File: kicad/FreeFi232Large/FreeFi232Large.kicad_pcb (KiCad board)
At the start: 2 copper layers, 40.6 x 53.3 mm, 165 parts, among them J1 DB25-Female, J2 3V3-SERIAL, J3 HWFLOW, J4 USB_OTG, J5 ALT-POWER, SW1 B3S-1100, U1 MAX3237, U2 ESP-12E, U3 LM1117-3.3

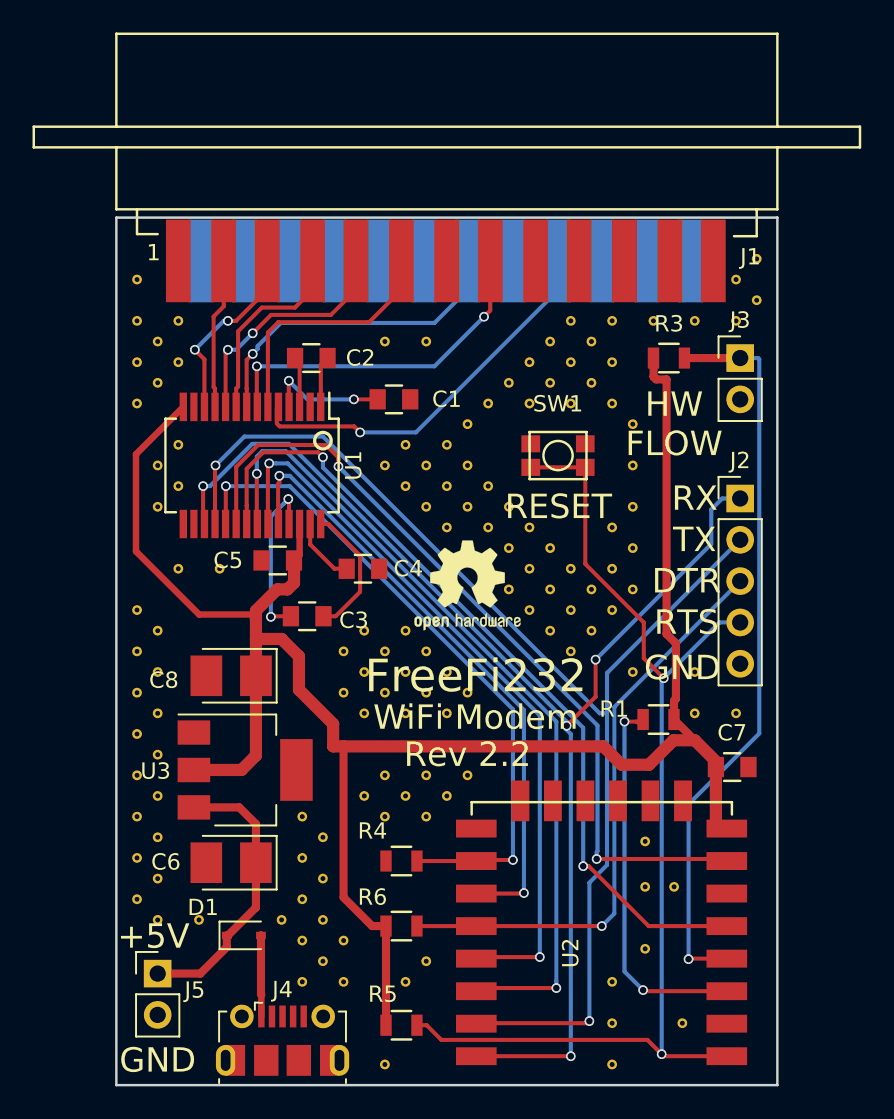
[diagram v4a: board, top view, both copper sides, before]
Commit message: Schematic corrections - pullup added on RX programming port, GPIOs adjusted.
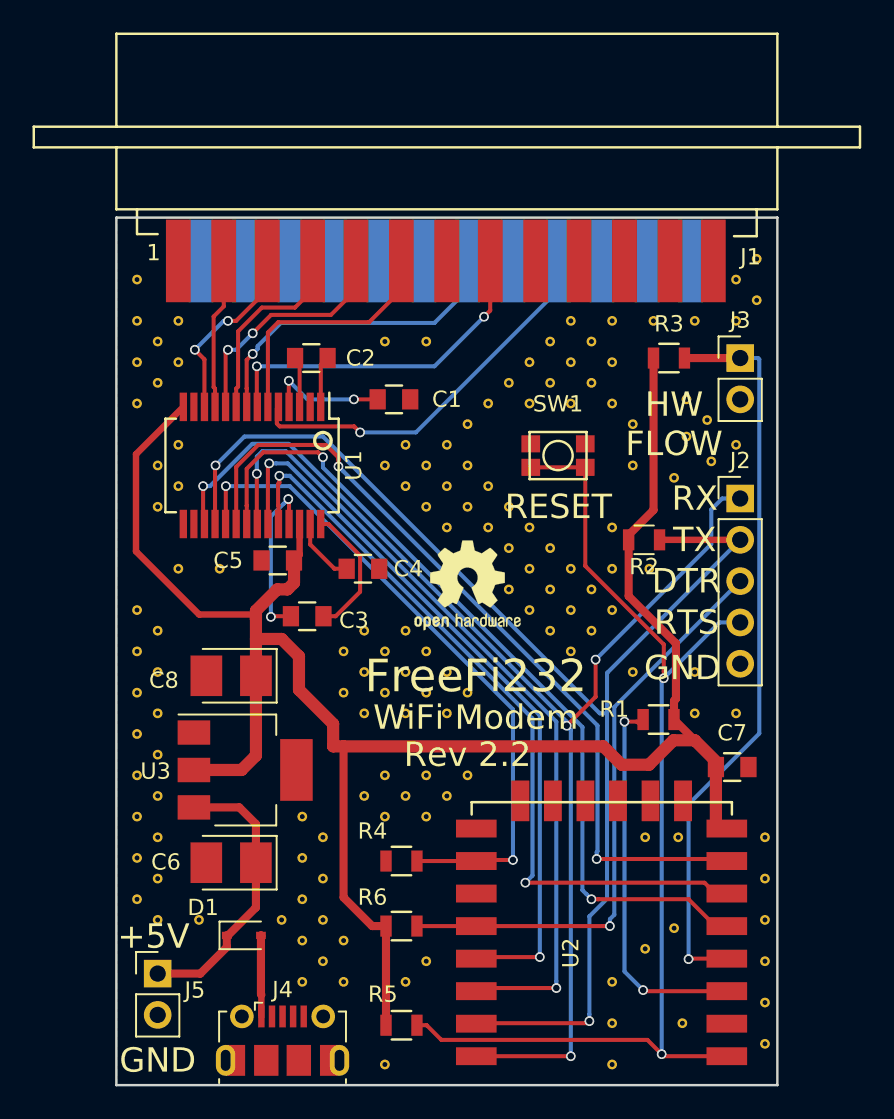
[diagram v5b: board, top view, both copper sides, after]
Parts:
- removed the REF** at (161.3, 101.6)
- removed the REF** at (161.3, 99.1)
- removed the REF** at (161.3, 96.5)
- removed the REF** at (162.1, 117.1)
- removed the REF** at (163.8, 119.9)
- removed the REF** at (162.1, 119.9)
- added R2: 10K, Resistors_SMD:R_0805, F.Cu at (162.0, 98.6)
- added REF**: VIA-0.6mm, stitchingVIA:VIA-0.6mm, F.Cu at (163.8, 122.4)
- added REF**: VIA-0.6mm, stitchingVIA:VIA-0.6mm, F.Cu at (163.8, 94.7)
- added REF**: VIA-0.6mm, stitchingVIA:VIA-0.6mm, F.Cu at (166.1, 93.7)
- added REF**: VIA-0.6mm, stitchingVIA:VIA-0.6mm, F.Cu at (167.6, 92.7)
- added REF**: VIA-0.6mm, stitchingVIA:VIA-0.6mm, F.Cu at (165.9, 91.2)
- added REF**: VIA-0.6mm, stitchingVIA:VIA-0.6mm, F.Cu at (164.6, 92.2)
- added REF**: VIA-0.6mm, stitchingVIA:VIA-0.6mm, F.Cu at (164.6, 89.9)
- added REF**: VIA-0.6mm, stitchingVIA:VIA-0.6mm, F.Cu at (162.3, 100.3)
- added REF**: VIA-0.6mm, stitchingVIA:VIA-0.6mm, F.Cu at (164.1, 116.8)
- added REF**: VIA-0.6mm, stitchingVIA:VIA-0.6mm, F.Cu at (162.1, 116.8)
- added REF**: VIA-0.6mm, stitchingVIA:VIA-0.6mm, F.Cu at (169.4, 116.8)
- added REF**: VIA-0.6mm, stitchingVIA:VIA-0.6mm, F.Cu at (169.4, 129.5)
- added REF**: VIA-0.6mm, stitchingVIA:VIA-0.6mm, F.Cu at (169.4, 127.0)
- added REF**: VIA-0.6mm, stitchingVIA:VIA-0.6mm, F.Cu at (169.4, 124.5)
- added REF**: VIA-0.6mm, stitchingVIA:VIA-0.6mm, F.Cu at (169.4, 121.9)
- added REF**: VIA-0.6mm, stitchingVIA:VIA-0.6mm, F.Cu at (169.4, 119.4)
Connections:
- U1 pad 24: GPIO2 -> GPIO12
- U2 pad 11: GPIO2 -> Net-(U2-Pad11)
- U2 pad 6: Net-(U2-Pad6) -> GPIO12
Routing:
- net GPIO12: track 0.00 -> 47.0 mm, vias 0 -> 2
- net GPIO2: track 37.5 -> 0.00 mm, vias 2 -> 0
- net RXD0: track 75.2 -> 80.2 mm
- net +3V3: track 122.9 -> 123.8 mm
- net GPIO14: track 50.1 -> 51.0 mm

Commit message: Error corrected in schematic and PCB. Gerbers updated.
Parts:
- added REF**: VIA-0.6mm, stitchingVIA:VIA-0.6mm, F.Cu at (152.4, 92.7)
- added REF**: VIA-0.6mm, stitchingVIA:VIA-0.6mm, F.Cu at (156.2, 96.5)
- added REF**: VIA-0.6mm, stitchingVIA:VIA-0.6mm, F.Cu at (162.6, 96.3)
- moved REF** 5.24 mm to (165.1, 96.5)
- moved REF** 4.82 mm to (164.6, 98.8)
- moved REF** 0.92 mm to (160.5, 93.5)
- moved R2 0.13 mm to (162.1, 98.6)
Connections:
- R2 pad 2: +3V3 -> GND
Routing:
- net RXD0: track 80.2 -> 75.2 mm
- net +3V3: track 123.8 -> 125.2 mm
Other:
- board text added: "Rev 2.4"
- board text removed: "Rev 2.2"
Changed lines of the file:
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@@
 (kicad_pcb (version 4) (host pcbnew 4.0.7)
   (general
-    (links 217)
-    (no_connects 0)
+    (links 227)
+    (no_connects 1)
     (area 124.184999 67.161999 175.535001 139.277001)
     (thickness 1.6)
     (drawings 19)
-    (tracks 329)
+    (tracks 330)
     (zones 0)
-    (modules 176)
+    (modules 179)
     (nets 58)
   )
@@
   )
   (setup
-    (last_trace_width 0.25)
+    (last_trace_width 0.5)
     (user_trace_width 0.4)
     (user_trace_width 0.5)
@@
   )
   (module stitchingVIA:VIA-0.6mm (layer F.Cu)
+    (at 152.4 92.71)
+    (zone_connect 2)
+    (fp_text reference REF** (at 0 0.5) (layer F.SilkS) hide
+      (effects (font (size 1 1) (thickness 0.15)))
+    )
+    (fp_text value VIA-0.6mm (at 0 -0.5) (layer F.Fab) hide
+      (effects (font (size 1 1) (thickness 0.15)))
+    )
+    (pad 1 thru_hole circle (at 0 0) (size 0.6 0.6) (drill 0.3) (layers *.Cu)
+      (net 5 GND) (zone_connect 2))
+  )
+  (module stitchingVIA:VIA-0.6mm (layer F.Cu)
+    (at 156.21 96.52)
+    (zone_connect 2)
+    (fp_text reference REF** (at 0 0.5) (layer F.SilkS) hide
+      (effects (font (size 1 1) (thickness 0.15)))
+    )
+    (fp_text value VIA-0.6mm (at 0 -0.5) (layer F.Fab) hide
+      (effects (font (size 1 1) (thickness 0.15)))
+    )
+    (pad 1 thru_hole circle (at 0 0) (size 0.6 0.6) (drill 0.3) (layers *.Cu)
+      (net 5 GND) (zone_connect 2))
+  )
+  (module stitchingVIA:VIA-0.6mm (layer F.Cu)
+    (at 162.56 96.266)
+    (zone_connect 2)
+    (fp_text reference REF** (at 0 0.5) (layer F.SilkS) hide
+      (effects (font (size 1 1) (thickness 0.15)))
+    )
+    (fp_text value VIA-0.6mm (at 0 -0.5) (layer F.Fab) hide
+      (effects (font (size 1 1) (thickness 0.15)))
+    )
+    (pad 1 thru_hole circle (at 0 0) (size 0.6 0.6) (drill 0.3) (layers *.Cu)
+      (net 5 GND) (zone_connect 2))
+  )
+  (module stitchingVIA:VIA-0.6mm (layer F.Cu)
     (at 163.83 122.428)
     (zone_connect 2)
@@
   )
   (module stitchingVIA:VIA-0.6mm (layer F.Cu)
-    (at 160.02 100.33)
+    (at 164.592 98.806)
     (zone_connect 2)
     (fp_text reference REF** (at 0 0.5) (layer F.SilkS) hide
@@
   )
   (module stitchingVIA:VIA-0.6mm (layer F.Cu)
-    (at 160.02 97.79)
+    (at 165.1 96.52)
     (zone_connect 2)
     (fp_text reference REF** (at 0 0.5) (layer F.SilkS) hide
@@
   )
   (module stitchingVIA:VIA-0.6mm (layer F.Cu)
-    (at 161.29 93.98)
+    (at 160.528 93.472)
     (zone_connect 2)
     (fp_text reference REF** (at 0 0.5) (layer F.SilkS) hide
@@
     (tags "resistor 0805")
     (attr smd)
-    (fp_text reference R3 (at 0 -2.1) (layer F.SilkS)
+    (fp_text reference R3 (at 0.315 -1.778) (layer F.SilkS)
       (effects (font (size 1 1) (thickness 0.15)))
     )
@@
   )
   (module Resistors_SMD:R_0805 (layer F.Cu)
-    (at 161.986 98.552 180)
+    (at 162.118 98.552 180)
     (descr "Resistor SMD 0805, reflow soldering, Vishay (see dcrcw.pdf)")
     (tags "resistor 0805")
     (attr smd)
-    (fp_text reference R2 (at 0 -1.65 180) (layer F.SilkS)
+    (fp_text reference R2 (at 1.336 -1.778 180) (layer F.SilkS)
       (effects (font (size 1 1) (thickness 0.15)))
     )
@@
       (net 17 RXD0))
     (pad 2 smd rect (at 0.95 0 180) (size 0.7 1.3) (layers F.Cu F.Paste F.Mask)
-      (net 6 +3V3))
+      (net 5 GND))
     (model ${KISYS3DMOD}/Resistors_SMD.3dshapes/R_0805.wrl
       (at (xyz 0 0 0))
@@
     )
   )
-  (gr_text "Rev 2.2" (at 151.13 111.76) (layer F.SilkS)
+  (gr_text "Rev 2.4" (at 151.13 111.76) (layer F.SilkS)
     (effects (font (size 1.5 1.5) (thickness 0.3)))
   )
@@
   (segment (start 144.525501 101.746999) (end 143.0215 103.251) (width 0.25) (layer F.Cu) (net 4))
   (segment (start 152.37 116.302) (end 151.354 116.302) (width 0.25) (layer F.Cu) (net 5) (status 30))
-  (segment (start 162.565 87.376) (end 162.565 96.723) (width 0.5) (layer F.Cu) (net 6))
-  (segment (start 162.565 96.723) (end 161.036 98.252) (width 0.5) (layer F.Cu) (net 6))
-  (segment (start 161.036 98.252) (end 161.036 98.552) (width 0.5) (layer F.Cu) (net 6))
+  (segment (start 161.036 98.252) (end 161.036 98.552) (width 0.5) (layer F.Cu) (net 5))
   (segment (start 163.825 109.601) (end 163.825 108.451) (width 0.5) (layer F.Cu) (net 6))
+  (segment (start 163.945001 104.922003) (end 159.258 100.235002) (width 0.5) (layer F.Cu) (net 6))
   (segment (start 163.825 108.451) (end 163.945001 108.330999) (width 0.5) (layer F.Cu) (net 6))
   (segment (start 163.945001 108.330999) (end 163.945001 104.922003) (width 0.5) (layer F.Cu) (net 6))
-  (segment (start 163.945001 104.922003) (end 161.036 102.013002) (width 0.5) (layer F.Cu) (net 6))
-  (segment (start 161.036 102.013002) (end 161.036 98.552) (width 0.5) (layer F.Cu) (net 6))
+  (segment (start 159.258 100.235002) (end 159.258 97.122002) (width 0.5) (layer F.Cu) (net 6))
+  (segment (start 159.258 97.122002) (end 162.565 93.815002) (width 0.5) (layer F.Cu) (net 6))
+  (segment (start 162.565 93.815002) (end 162.565 88.526) (width 0.5) (layer F.Cu) (net 6))
+  (segment (start 162.565 88.526) (end 162.565 87.376) (width 0.5) (layer F.Cu) (net 6))
   (segment (start 142.868488 111.252) (end 142.868488 109.87349) (width 0.75) (layer F.Cu) (net 6))
   (segment (start 140.767333 107.772335) (end 140.767333 105.715333) (width 0.75) (layer F.Cu) (net 6))
@@
   (segment (start 158.623 121.702005) (end 158.623 127.718736) (width 0.25) (layer B.Cu) (net 17))
   (segment (start 159.706988 109.22) (end 159.706988 120.618017) (width 0.25) (layer B.Cu) (net 17))
-  (segment (start 162.936 98.552) (end 167.894 98.552) (width 0.4) (layer F.Cu) (net 17))
   (segment (start 159.258 109.22) (end 142.23898 92.20098) (width 0.25) (layer B.Cu) (net 17))
   (segment (start 142.23898 92.20098) (end 137.41502 92.20098) (width 0.25) (layer B.Cu) (net 17))
@@
   (segment (start 161.989 126.302) (end 161.925 126.238) (width 0.25) (layer F.Cu) (net 18))
   (via (at 161.925 126.238) (size 0.6) (drill 0.4) (layers F.Cu B.Cu) (net 18))
-  (segment (start 163.195 104.98519) (end 163.195 106.636736) (width 0.25) (layer F.Cu) (net 19))
-  (segment (start 158.369 94.0965) (end 158.369 100.15919) (width 0.25) (layer F.Cu) (net 19))
-  (segment (start 158.369 100.15919) (end 163.195 104.98519) (width 0.25) (layer F.Cu) (net 19))
+  (segment (start 158.369 94.0965) (end 157.988 94.4775) (width 0.25) (layer F.Cu) (net 19))
+  (segment (start 157.988 94.4775) (end 157.988 99.77819) (width 0.25) (layer F.Cu) (net 19))
   (segment (start 163.195 106.636736) (end 163.195 107.061) (width 0.25) (layer F.Cu) (net 19))
+  (segment (start 157.988 99.77819) (end 163.195 104.98519) (width 0.25) (layer F.Cu) (net 19))
+  (segment (start 163.195 104.98519) (end 163.195 106.636736) (width 0.25) (layer F.Cu) (net 19))
   (segment (start 163.195 107.061) (end 166.624 103.632) (width 0.25) (layer B.Cu) (net 19))
   (segment (start 166.624 103.632) (end 167.894 103.632) (width 0.25) (layer B.Cu) (net 19) (status 20))

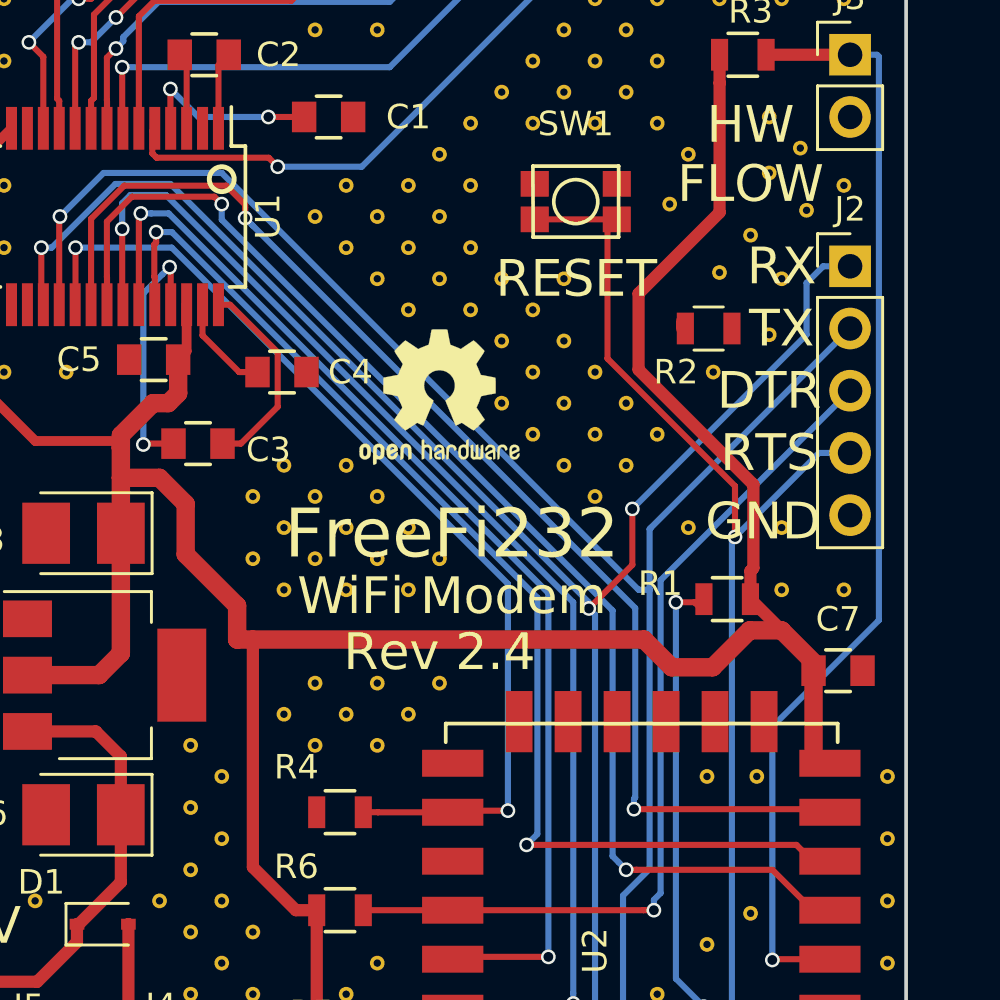
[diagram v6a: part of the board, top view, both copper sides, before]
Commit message: Version 2.5 of PCB/Schematic - current limiting resistor between MAX3237 and ESP12
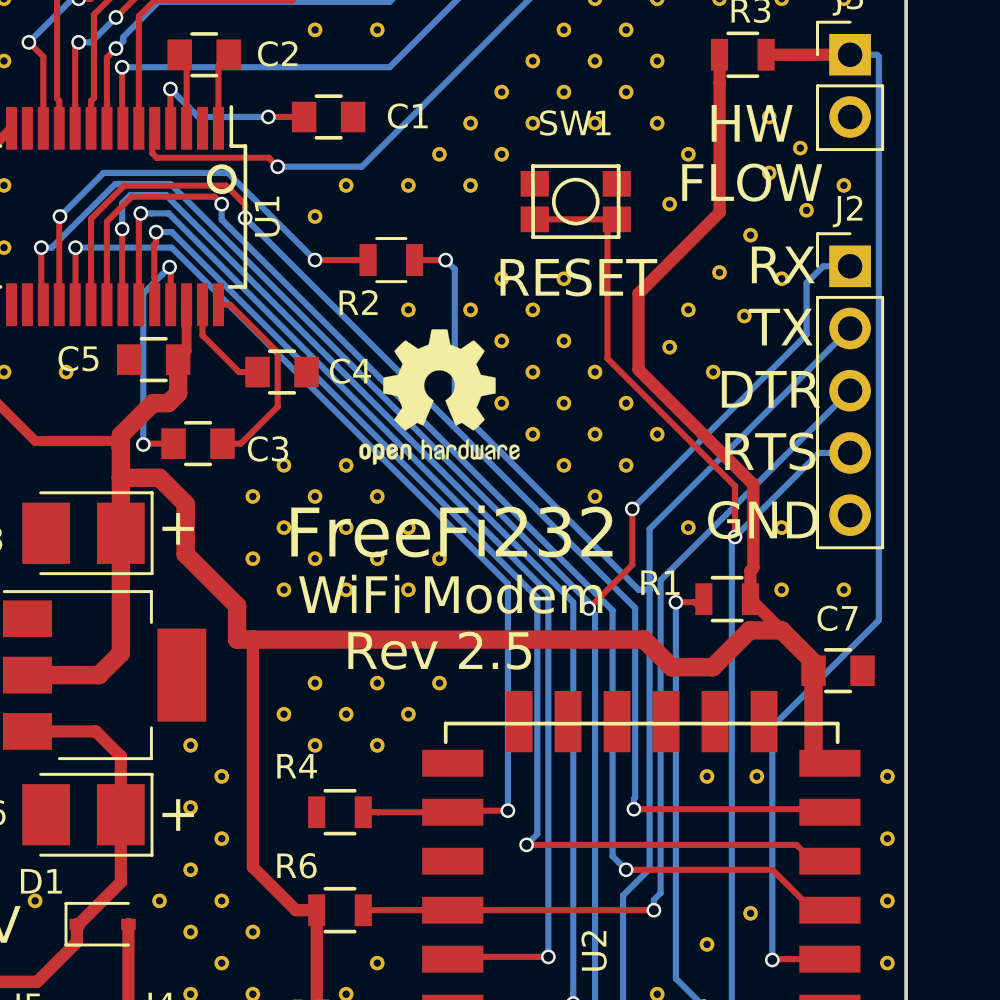
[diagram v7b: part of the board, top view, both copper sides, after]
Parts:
- removed the REF** at (164.6, 98.8)
- removed the REF** at (149.9, 95.2)
- removed the REF** at (148.6, 96.5)
- removed the REF** at (148.6, 94.0)
- R2: value 10K -> 300R
- moved REF** 14.2 mm to (161.3, 97.8)
- moved R2 13.3 mm to (149.2, 95.8)
- moved REF** 11.5 mm to (163.6, 98.0), turned to 180 degrees
- moved REF** 9.80 mm to (160.5, 99.3), turned to 180 degrees
- moved REF** 3.59 mm to (153.7, 91.4), turned to 180 degrees
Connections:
- R2 pad 2: GND -> RXD0A
- U1 pad 18: RXD0 -> RXD0A
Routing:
- net RXD0A: track 0.00 -> 18.4 mm, vias 0 -> 2
- net RXD0: track 75.2 -> 58.2 mm
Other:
- board text added: "+"
- board text added: "Rev 2.5"
- board text removed: "Rev 2.4"
